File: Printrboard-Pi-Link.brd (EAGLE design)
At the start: 65 x 56 mm, 26 parts, among them J1 5566-4, J2 5566-6, J3 PIN20X2, J5 MKDSN1,5/6-5,08, Q2 BSS123, Q3 BSS123, Q4 BSS123, U1 74AHC1G32DCK, U2 LM2596SX-5.0/NOPB

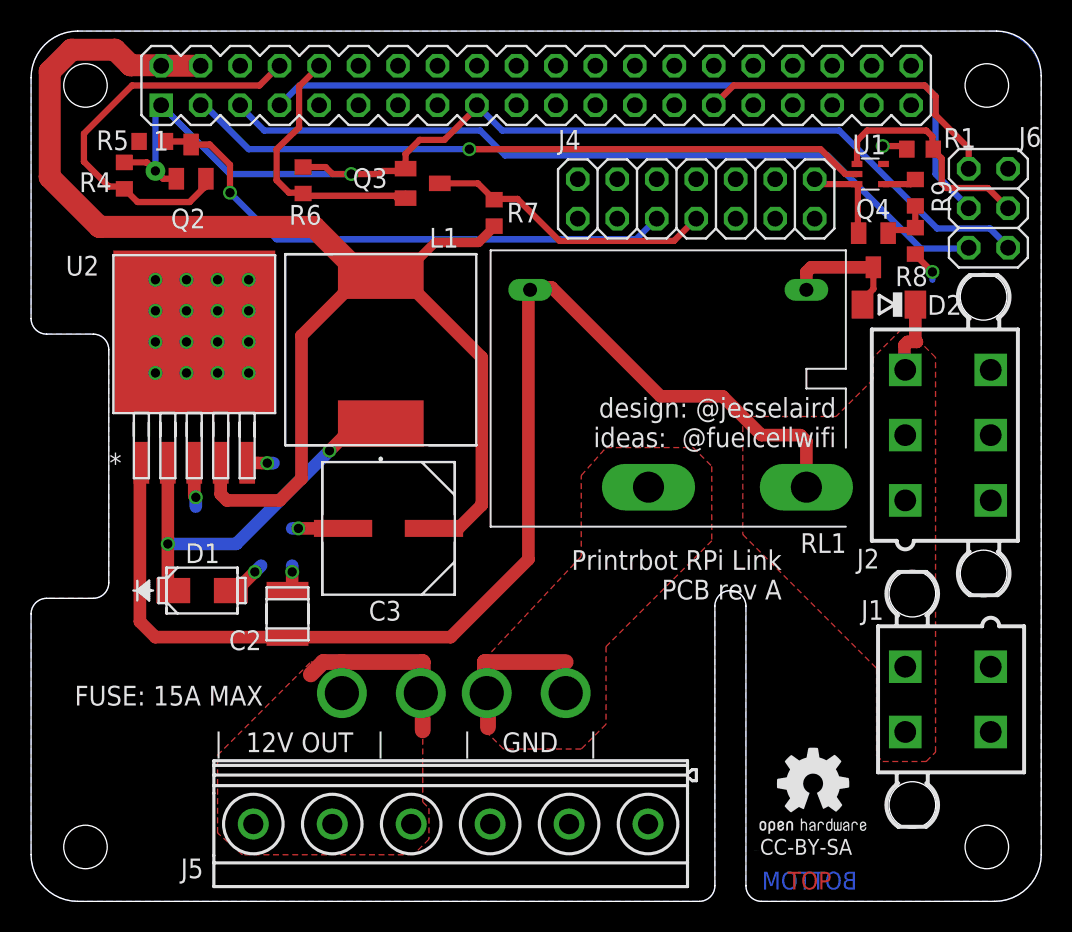
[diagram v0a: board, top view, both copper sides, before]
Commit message: Rev_B
Fixes missing 3v3 connection on NOR gate; reduces fuse size from ATO to
mini-ATO/automotive fuse.
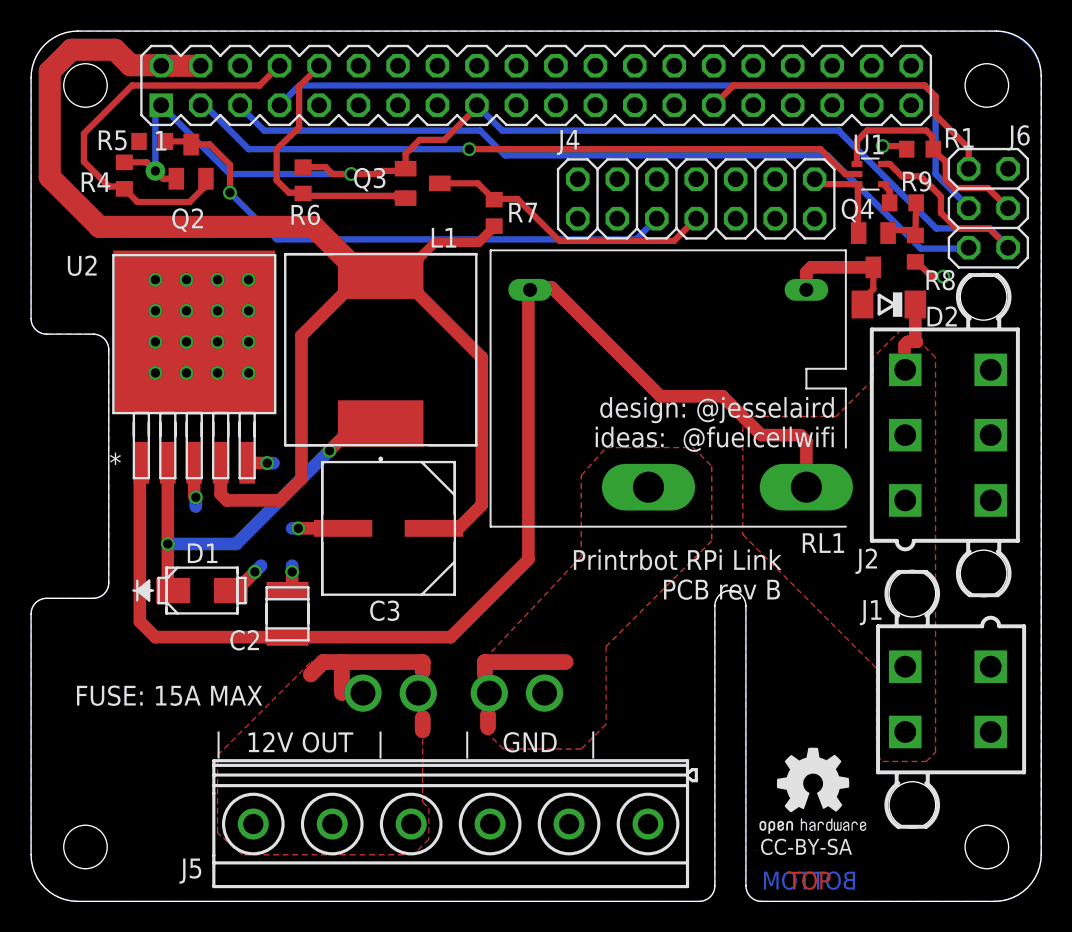
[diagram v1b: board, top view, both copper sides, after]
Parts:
- F1: value LITTELFUSE_ATO -> MINI-ATO; device jesse_laird:FUSE_ATO -> jesse_laird:BK-6011
- moved R9 1.03 mm to (56.1, 45.0), turned to 0 degrees
- moved R8 0.50 mm to (56.9, 42.0)
- turned F1 to 0 degrees
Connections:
- net N$2: now also F1.P$3
- net N$8: now also F1.P$1, F1.P$2; no longer F1.P$3
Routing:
- net N$9: track 0.00 -> 10.8 mm
- net N$7: track 3.29 -> 4.16 mm
- net N$3: track 2.17 -> 1.35 mm
- net GND: track 61.6 -> 62.1 mm
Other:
- board text added: "Printrbot RPi Link PCB rev B"
- board text removed: "Printrbot RPi Link PCB rev A"
